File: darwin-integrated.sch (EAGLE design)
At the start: 41 parts

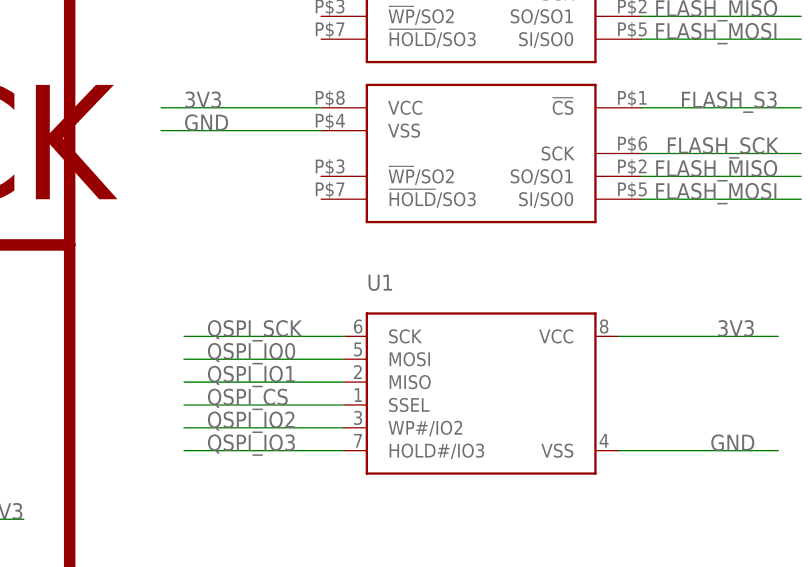
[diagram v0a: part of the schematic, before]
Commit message: Silk cleanup and other housecleaning.
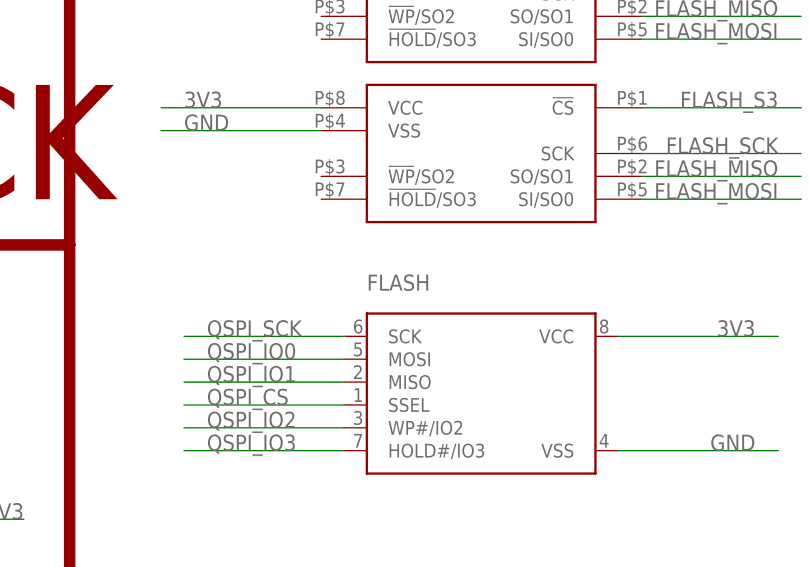
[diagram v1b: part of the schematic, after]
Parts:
- renumbered U$1 to BRAIN, U$2 to RTC, U1 to FLASH

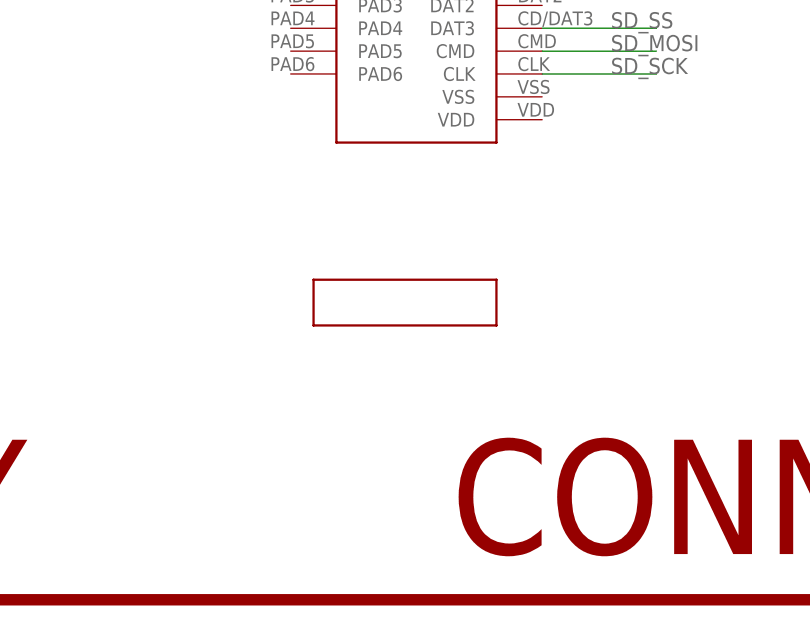
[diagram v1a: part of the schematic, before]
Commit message: Added screen contacts
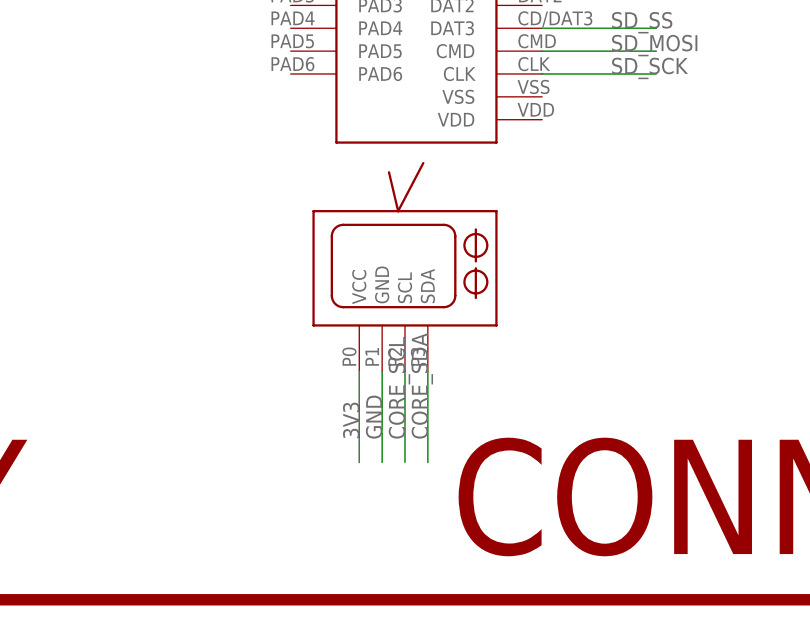
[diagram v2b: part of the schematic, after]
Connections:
- net 3V3: now also U$10.VCC
- net CORE_SCL: now also U$10.SCL
- net CORE_SDA: now also U$10.SDA
- net GND: now also U$10.GND
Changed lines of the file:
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@@
 <label x="142.24" y="17.78" size="1.778" layer="95"/>
+</segment>
+<segment>
+<pinref part="U$10" gate="G$1" pin="SDA"/>
+<wire x1="251.46" y1="-121.92" x2="251.46" y2="-132.08" width="0.1524" layer="91"/>
+<label x="251.46" y="-129.54" size="1.778" layer="95" rot="R90"/>
 </segment>
 </net>
@@
 <wire x1="154.94" y1="10.16" x2="144.78" y2="10.16" width="0.1524" layer="91"/>
 <label x="142.24" y="10.16" size="1.778" layer="95"/>
+</segment>
+<segment>
+<pinref part="U$10" gate="G$1" pin="SCL"/>
+<wire x1="248.92" y1="-121.92" x2="248.92" y2="-132.08" width="0.1524" layer="91"/>
+<label x="248.92" y="-129.54" size="1.778" layer="95" rot="R90"/>
 </segment>
 </net>
@@
 <wire x1="261.62" y1="58.42" x2="281.94" y2="58.42" width="0.1524" layer="91"/>
 <label x="279.4" y="58.42" size="1.778" layer="95" align="bottom-right"/>
+</segment>
+<segment>
+<pinref part="U$10" gate="G$1" pin="GND"/>
+<wire x1="246.38" y1="-121.92" x2="246.38" y2="-132.08" width="0.1524" layer="91"/>
+<label x="246.38" y="-129.54" size="1.778" layer="95" rot="R90"/>
 </segment>
 </net>
@@
 <label x="279.4" y="60.96" size="1.778" layer="95" align="bottom-right"/>
 </segment>
-</net>
+<segment>
+<pinref part="U$10" gate="G$1" pin="VCC"/>
+<wire x1="243.84" y1="-121.92" x2="243.84" y2="-132.08" width="0.1524" layer="91"/>
+<label x="243.84" y="-129.54" size="1.778" layer="95" rot="R90"/>
+</segment>
+</net>

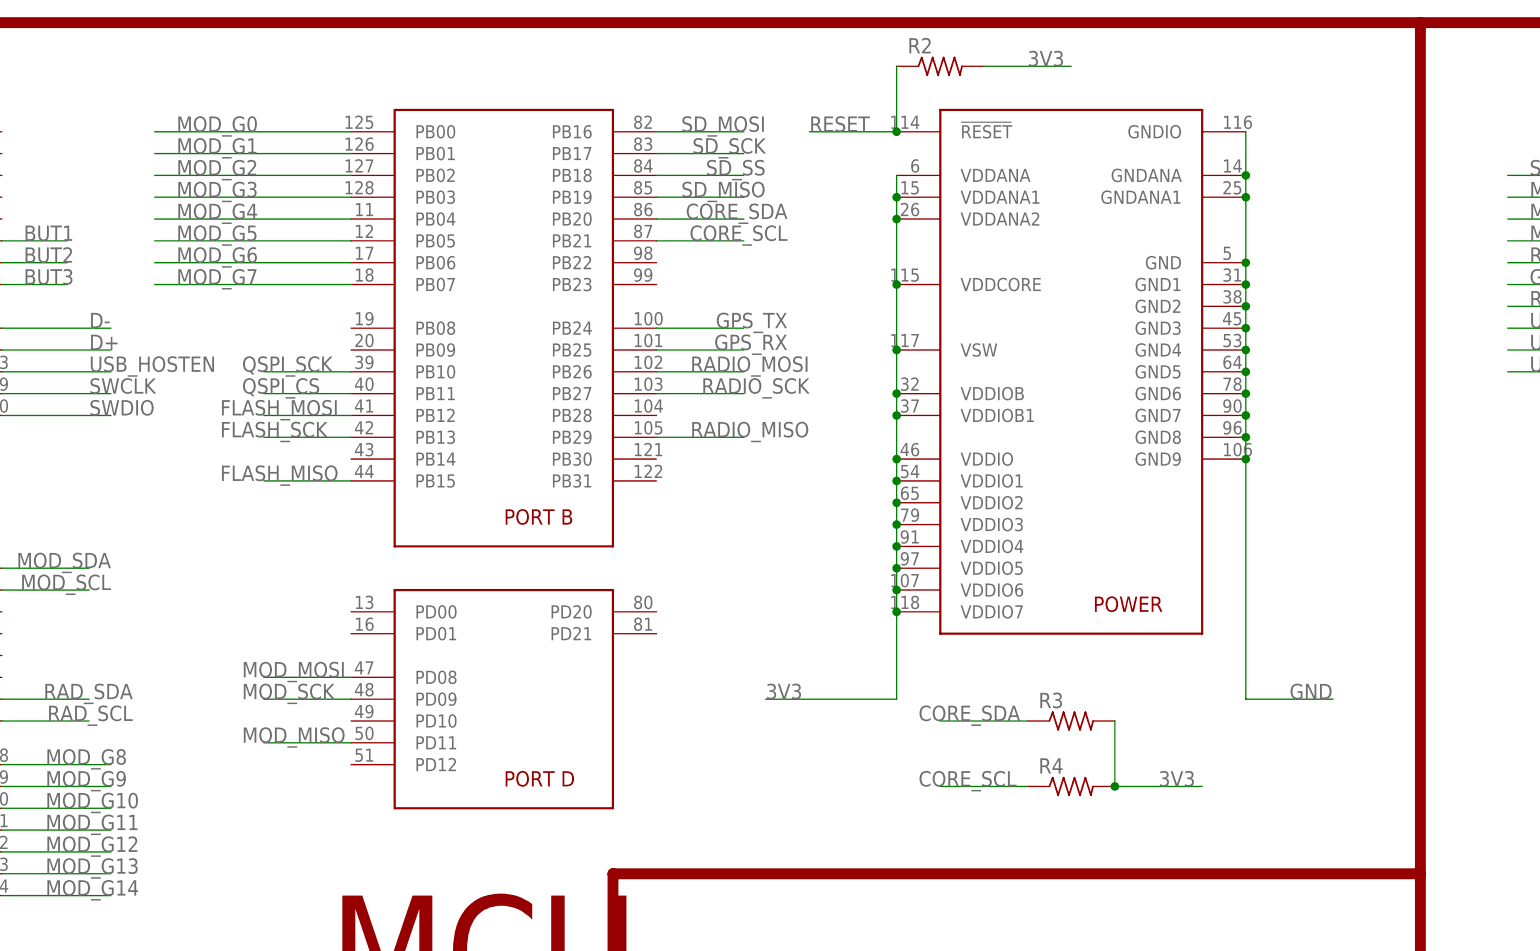
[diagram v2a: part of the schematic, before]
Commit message: Corrected VDDCORE and VSW errors.
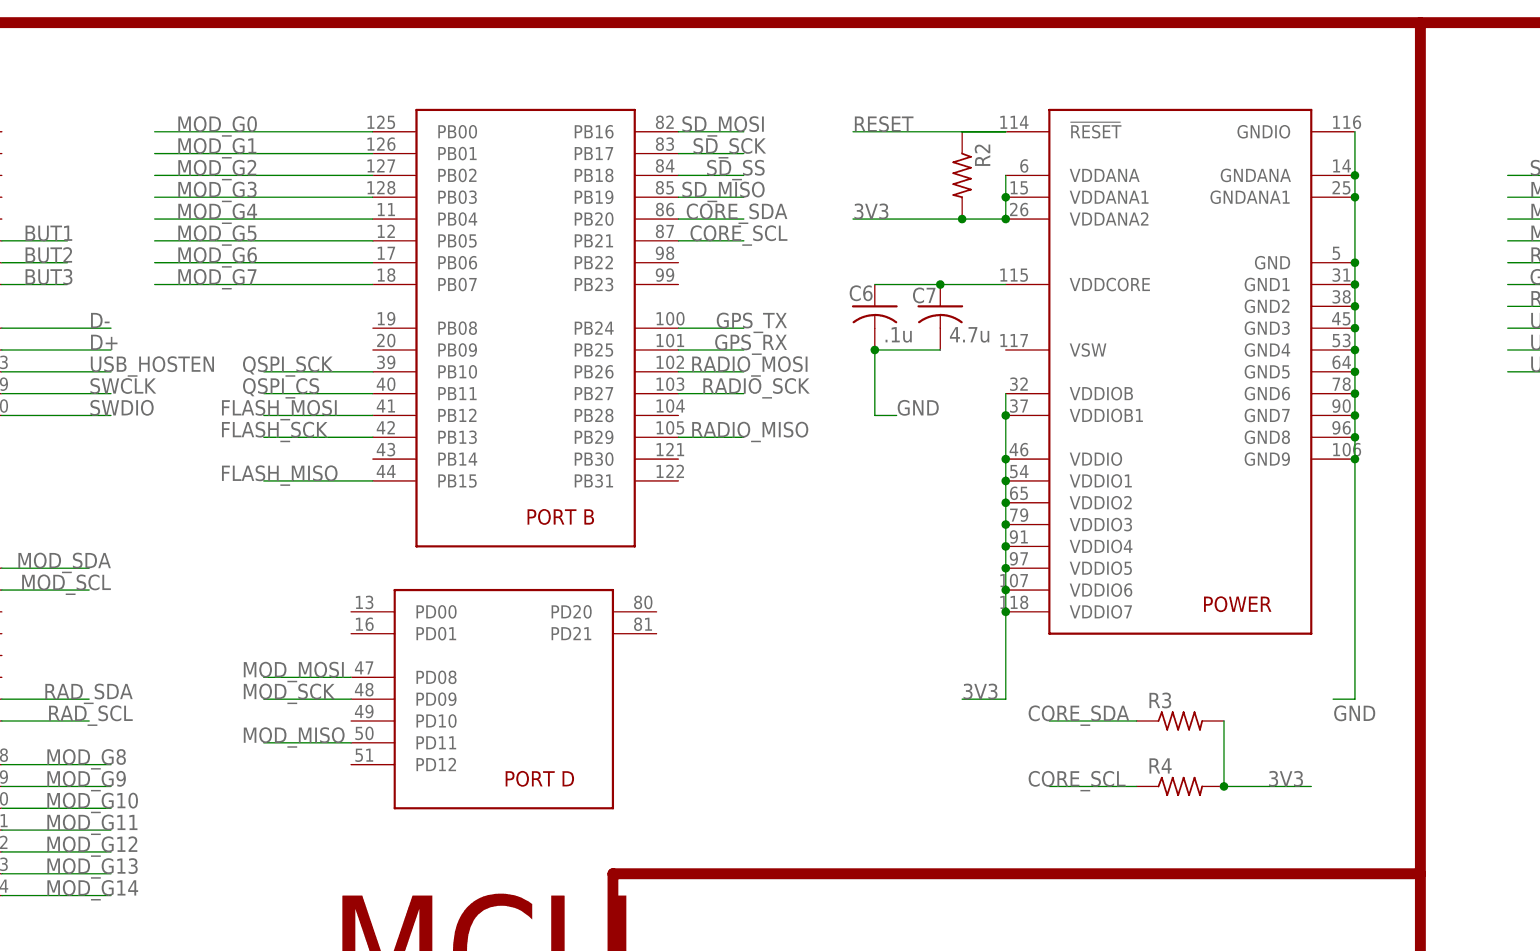
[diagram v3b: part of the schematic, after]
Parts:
- added C6: .1u, rcl:C-USC0603K
- added C7: 4.7u, rcl:C-USC0603K
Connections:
- new net N$6: BRAING$5.VDDCORE, C6.1, C7.1
- net 3V3: no longer BRAING$5.VDDCORE, BRAING$5.VSW
- net GND: now also C6.2, C7.2
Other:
- moved on the sheet: R2, R3, R4

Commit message: Added pullup resistor for QSPI Flash chip select.
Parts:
- added R5: (no value), rcl:R-US_R0603
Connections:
- net 3V3: now also R5.2
- net QSPI_CS: now also R5.1
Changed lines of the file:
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@@
 <part name="C6" library="rcl" library_urn="urn:adsk.eagle:library:334" deviceset="C-US" device="C0603K" package3d_urn="urn:adsk.eagle:package:23680/2" value=".1u"/>
 <part name="C7" library="rcl" library_urn="urn:adsk.eagle:library:334" deviceset="C-US" device="C0603K" package3d_urn="urn:adsk.eagle:package:23680/2" value="4.7u"/>
+<part name="R5" library="rcl" library_urn="urn:adsk.eagle:library:334" deviceset="R-US_" device="R0603" package3d_urn="urn:adsk.eagle:package:23555/3"/>
 </parts>
 <sheets>
@@
 <attribute name="VALUE" x="145.796" y="61.849" size="1.778" layer="96"/>
 </instance>
+<instance part="R5" gate="G$1" x="124.46" y="-114.3" smashed="yes">
+<attribute name="NAME" x="120.65" y="-112.8014" size="1.778" layer="95"/>
+<attribute name="VALUE" x="120.65" y="-117.602" size="1.778" layer="96"/>
+</instance>
 </instances>
 <busses>
@@
 <segment>
 <pinref part="FLASH" gate="G$1" pin="SSEL"/>
-<wire x1="137.16" y1="-99.06" x2="119.38" y2="-99.06" width="0.1524" layer="91"/>
+<wire x1="137.16" y1="-99.06" x2="114.3" y2="-99.06" width="0.1524" layer="91"/>
 <label x="121.92" y="-99.06" size="1.778" layer="95"/>
+<pinref part="R5" gate="G$1" pin="1"/>
+<wire x1="114.3" y1="-99.06" x2="114.3" y2="-114.3" width="0.1524" layer="91"/>
+<wire x1="114.3" y1="-114.3" x2="119.38" y2="-114.3" width="0.1524" layer="91"/>
 </segment>
 </net>
@@
 <wire x1="147.32" y1="76.2" x2="134.62" y2="76.2" width="0.1524" layer="91"/>
 </segment>
-</net>
+<segment>
+<pinref part="R5" gate="G$1" pin="2"/>
+<wire x1="129.54" y1="-114.3" x2="137.16" y2="-114.3" width="0.1524" layer="91"/>
+<label x="132.08" y="-114.3" size="1.778" layer="95"/>
+</segment>
+</net>

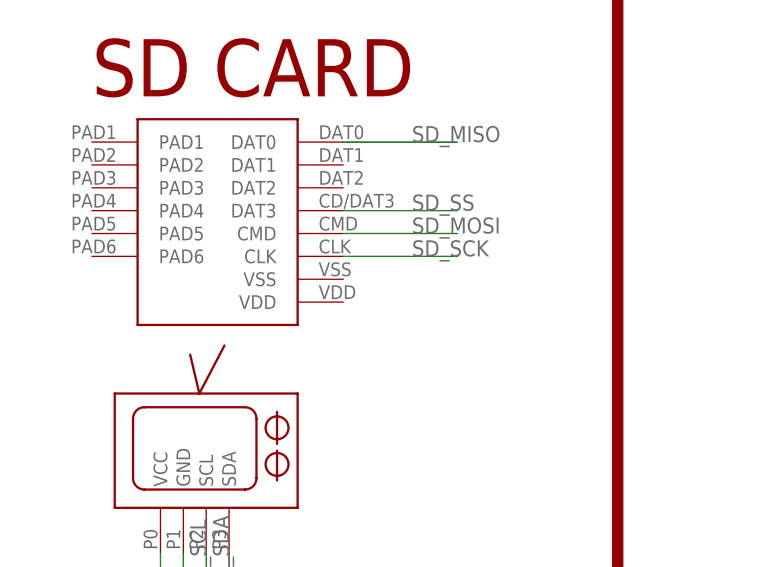
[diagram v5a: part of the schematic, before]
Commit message: Fixed SD Power Disconnect.
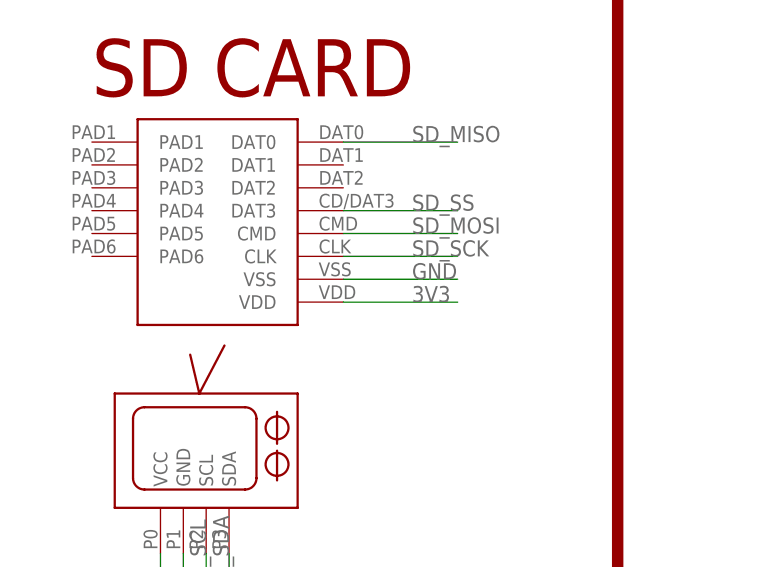
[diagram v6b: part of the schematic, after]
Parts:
- LOWER, UPPER: value MOLEX-15-91-2200 -> MOLEX-15-91-2200F; device Conservify:MOLEX-15-91-2200 -> Conservify:MOLEX-15-91-2200F
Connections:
- net 3V3: now also U$9.VDD
- net GND: now also U$9.VSS
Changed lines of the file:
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@@
 <part name="BRAIN" library="microbuilder" deviceset="SAMD51PXXA" device=""/>
 <part name="C1" library="rcl" library_urn="urn:adsk.eagle:library:334" deviceset="C-US" device="C0603K" package3d_urn="urn:adsk.eagle:package:23680/2"/>
-<part name="RTC" library="Conservify" deviceset="PCF85363ATT" device="" package3d_urn="urn:adsk.eagle:package:10002685/1"/>
-<part name="U$3" library="Conservify" deviceset="TC58CVG1S3HRAIG" device=""/>
-<part name="U$4" library="Conservify" deviceset="TC58CVG1S3HRAIG" device=""/>
-<part name="U$5" library="Conservify" deviceset="TC58CVG1S3HRAIG" device=""/>
-<part name="U$6" library="Conservify" deviceset="TC58CVG1S3HRAIG" device=""/>
-<part name="U$7" library="Conservify" deviceset="DSK-3R3H204T614-H2L" device=""/>
+<part name="RTC" library="Conservify" library_urn="urn:adsk.eagle:library:11839183" deviceset="PCF85363ATT" device="" package3d_urn="urn:adsk.eagle:package:10002685/1"/>
+<part name="U$3" library="Conservify" library_urn="urn:adsk.eagle:library:11839183" deviceset="TC58CVG1S3HRAIG" device="" package3d_urn="urn:adsk.eagle:package:11839247/1"/>
+<part name="U$4" library="Conservify" library_urn="urn:adsk.eagle:library:11839183" deviceset="TC58CVG1S3HRAIG" device="" package3d_urn="urn:adsk.eagle:package:11839247/1"/>
+<part name="U$5" library="Conservify" library_urn="urn:adsk.eagle:library:11839183" deviceset="TC58CVG1S3HRAIG" device="" package3d_urn="urn:adsk.eagle:package:11839247/1"/>
+<part name="U$6" library="Conservify" library_urn="urn:adsk.eagle:library:11839183" deviceset="TC58CVG1S3HRAIG" device="" package3d_urn="urn:adsk.eagle:package:11839247/1"/>
+<part name="U$7" library="Conservify" library_urn="urn:adsk.eagle:library:11839183" deviceset="DSK-3R3H204T614-H2L" device="" package3d_urn="urn:adsk.eagle:package:11839248/2"/>
 <part name="D1" library="diode" library_urn="urn:adsk.eagle:library:210" deviceset="DIODE-" device="SMB" package3d_urn="urn:adsk.eagle:package:43404/2"/>
 <part name="R1" library="rcl" library_urn="urn:adsk.eagle:library:334" deviceset="R-US_" device="R0603" package3d_urn="urn:adsk.eagle:package:23555/3"/>
 <part name="FLASH" library="microbuilder" deviceset="SPIFLASH_SOIC8" device="208MIL"/>
-<part name="U$8" library="Conservify" deviceset="MOLEX-47491-0001" device=""/>
-<part name="U$9" library="Conservify" deviceset="DM3D-SF" device=""/>
-<part name="U$10" library="Conservify" deviceset="SCREEN" device=""/>
+<part name="U$8" library="Conservify" library_urn="urn:adsk.eagle:library:11839183" deviceset="MOLEX-47491-0001" device="" package3d_urn="urn:adsk.eagle:package:11839249/2"/>
+<part name="U$9" library="Conservify" library_urn="urn:adsk.eagle:library:11839183" deviceset="DM3D-SF" device="" package3d_urn="urn:adsk.eagle:package:11839251/1"/>
+<part name="U$10" library="Conservify" library_urn="urn:adsk.eagle:library:11839183" deviceset="SCREEN" device="" package3d_urn="urn:adsk.eagle:package:11839246/5"/>
 <part name="C2" library="rcl" library_urn="urn:adsk.eagle:library:334" deviceset="C-US" device="C0603K" package3d_urn="urn:adsk.eagle:package:23680/2"/>
 <part name="C3" library="rcl" library_urn="urn:adsk.eagle:library:334" deviceset="C-US" device="C0603K" package3d_urn="urn:adsk.eagle:package:23680/2"/>
@@
 <part name="C21" library="rcl" library_urn="urn:adsk.eagle:library:334" deviceset="C-US" device="C0603K" package3d_urn="urn:adsk.eagle:package:23680/2"/>
 <part name="C22" library="rcl" library_urn="urn:adsk.eagle:library:334" deviceset="C-US" device="C0603K" package3d_urn="urn:adsk.eagle:package:23680/2"/>
-<part name="UPPER" library="Conservify" deviceset="MOLEX-15-91-2200" device=""/>
-<part name="LOWER" library="Conservify" deviceset="MOLEX-15-91-2200" device=""/>
-<part name="BTN1" library="Conservify" deviceset="EVP-AEJB2A" device=""/>
-<part name="BTN2" library="Conservify" deviceset="EVP-AEJB2A" device=""/>
-<part name="BTN3" library="Conservify" deviceset="EVP-AEJB2A" device=""/>
-<part name="U$14" library="Conservify" deviceset="ABS07W" device=""/>
-<part name="UTEMP" library="Conservify" deviceset="PCT2075" device="" package3d_urn="urn:adsk.eagle:package:11214694/1"/>
+<part name="UPPER" library="Conservify" library_urn="urn:adsk.eagle:library:11839183" deviceset="MOLEX-15-91-2200" device="F" package3d_urn="urn:adsk.eagle:package:11853535/2" value="MOLEX-15-91-2200F"/>
+<part name="LOWER" library="Conservify" library_urn="urn:adsk.eagle:library:11839183" deviceset="MOLEX-15-91-2200" device="F" package3d_urn="urn:adsk.eagle:package:11853535/2" value="MOLEX-15-91-2200F"/>
+<part name="BTN1" library="Conservify" library_urn="urn:adsk.eagle:library:11839183" deviceset="EVP-AEJB2A" device="" package3d_urn="urn:adsk.eagle:package:11839244/1"/>
+<part name="BTN2" library="Conservify" library_urn="urn:adsk.eagle:library:11839183" deviceset="EVP-AEJB2A" device="" package3d_urn="urn:adsk.eagle:package:11839244/1"/>
+<part name="BTN3" library="Conservify" library_urn="urn:adsk.eagle:library:11839183" deviceset="EVP-AEJB2A" device="" package3d_urn="urn:adsk.eagle:package:11839244/1"/>
+<part name="U$14" library="Conservify" library_urn="urn:adsk.eagle:library:11839183" deviceset="ABS07W" device="" package3d_urn="urn:adsk.eagle:package:11839243/1"/>
+<part name="UTEMP" library="Conservify" library_urn="urn:adsk.eagle:library:11839183" deviceset="PCT2075" device="" package3d_urn="urn:adsk.eagle:package:11214694/2"/>
 <part name="R2" library="rcl" library_urn="urn:adsk.eagle:library:334" deviceset="R-US_" device="R0603" package3d_urn="urn:adsk.eagle:package:23555/3"/>
 <part name="R3" library="rcl" library_urn="urn:adsk.eagle:library:334" deviceset="R-US_" device="R0603" package3d_urn="urn:adsk.eagle:package:23555/3"/>
@@
 <wire x1="137.16" y1="53.34" x2="139.7" y2="53.34" width="0.1524" layer="91"/>
 </segment>
+<segment>
+<pinref part="U$9" gate="1" pin="VSS"/>
+<wire x1="264.16" y1="-91.44" x2="276.86" y2="-91.44" width="0.1524" layer="91"/>
+<label x="271.78" y="-91.44" size="1.778" layer="95"/>
+</segment>
 </net>
 <net name="3V3" class="0">
@@
 <label x="132.08" y="-114.3" size="1.778" layer="95"/>
 </segment>
-</net>
+<segment>
+<pinref part="U$9" gate="1" pin="VDD"/>
+<wire x1="264.16" y1="-93.98" x2="276.86" y2="-93.98" width="0.1524" layer="91"/>
+<label x="271.78" y="-93.98" size="1.778" layer="95"/>
+</segment>
+</net>
